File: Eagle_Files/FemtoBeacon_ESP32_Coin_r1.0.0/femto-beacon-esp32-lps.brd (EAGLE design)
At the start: 54.6 x 33 mm, 56 parts, among them IC1 ESP32-QFN_5X5

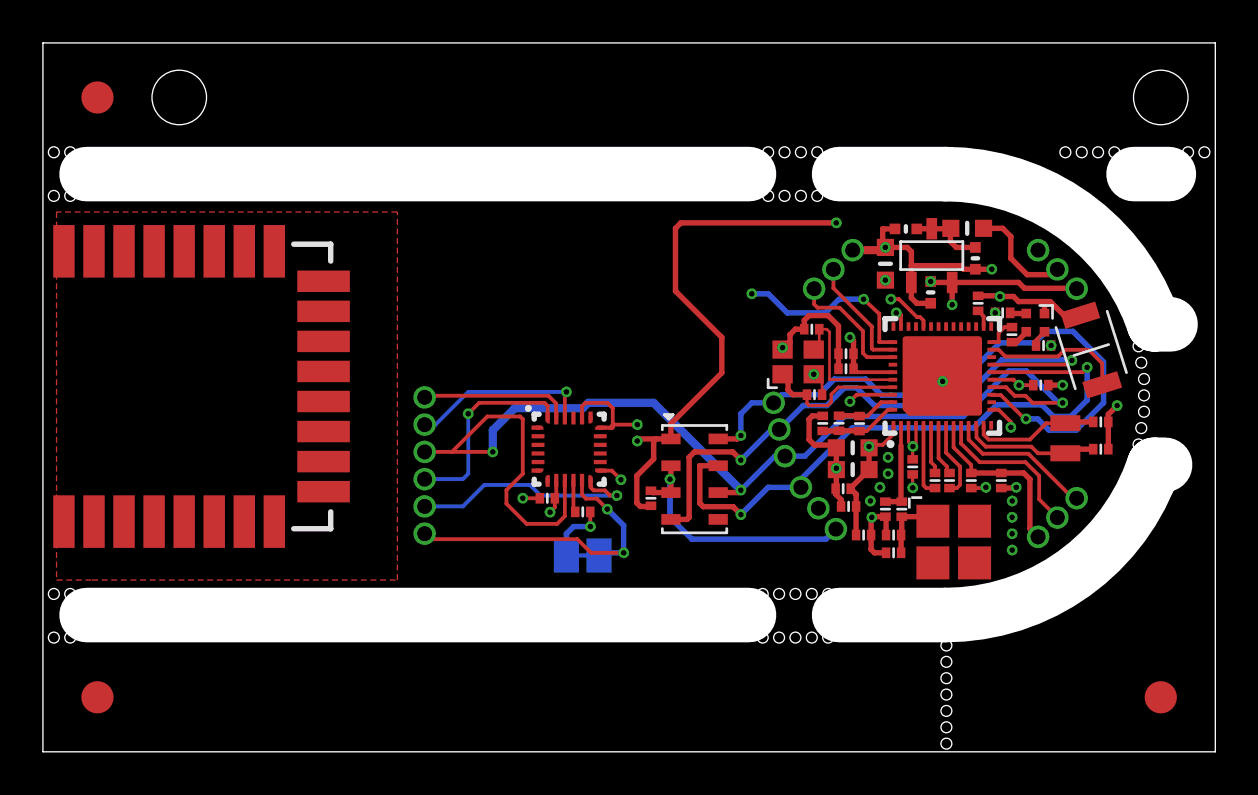
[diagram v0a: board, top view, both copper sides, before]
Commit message: Updating ESP32-WROOM-32 board. RGB Blue pin reassigned, and RGB pin 1 set to VCC instead of GND. LiPo connector pins were switched, corrected now.
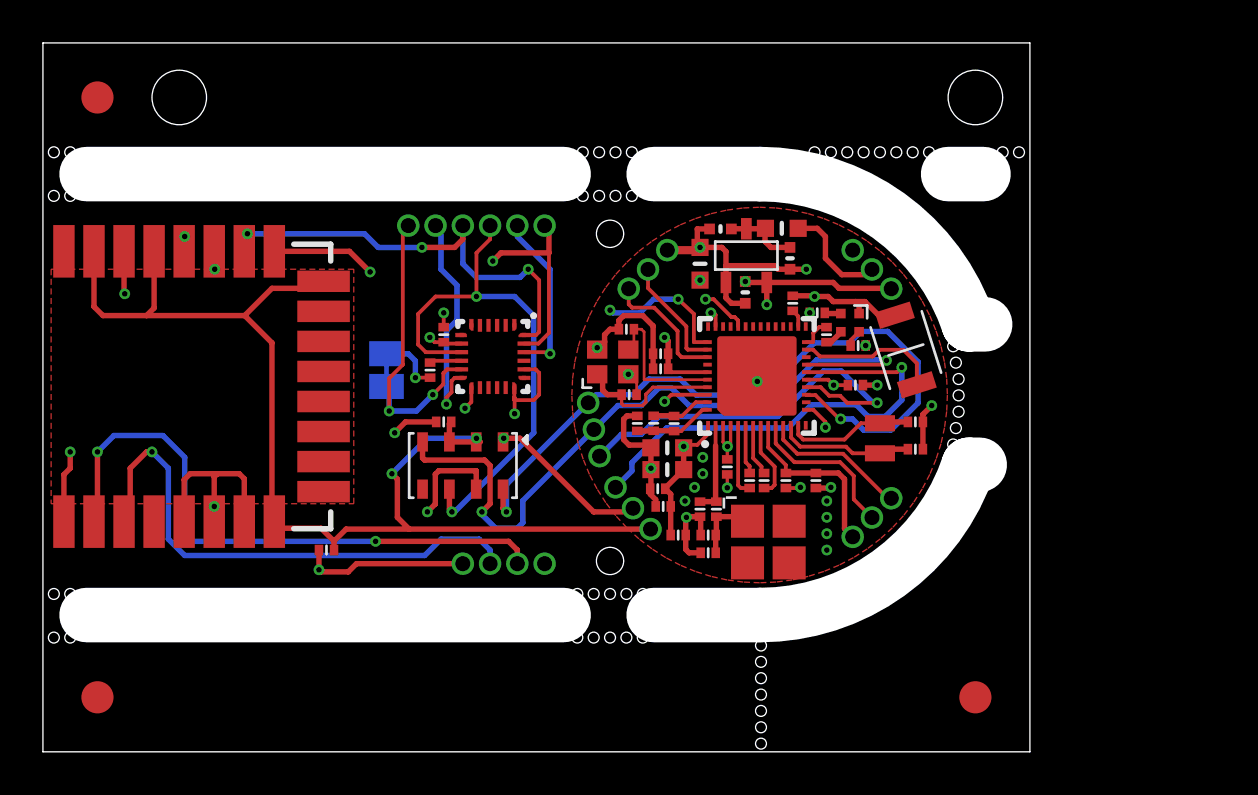
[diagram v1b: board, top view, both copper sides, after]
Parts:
- removed U$41: ICM-20948, icm-20948:QFN24_3X3
- removed U$9: MS5611-01BA03, freeimu:MS5611-01BA03
- added ALT1: MS5611-01BA03, freeimu:MS5611-01BA03
- added IMU1: ICM-20948, icm-20948:QFN24_3X3
- added R7: 4.7K, parts_0201:PART
- added U$39: 1X4_ROUND, pins_1.27mm_pitch:1X4_ROUND
- R6: value DNP -> 0
- moved SJ_FSYNC 12.6 mm to (16.0, 17.8), turned to 90 degrees
- moved C25 10.3 mm to (18.7, 15.4), turned to 0 degrees
- moved PIN_IMU_SPI 9.76 mm to (23.4, 24.5), turned to 270 degrees
- moved C29 9.71 mm to (18.0, 17.8), turned to 90 degrees
- moved C28 9.02 mm to (18.7, 19.4), turned to 270 degrees
- moved ANT1 8.64 mm to (33.8, 9.78)
- moved C1 8.64 mm to (28.6, 12.3)
- moved C10 8.64 mm to (29.1, 14.2)
- moved C11 8.64 mm to (29.1, 13.1)
- moved C12 8.64 mm to (28.9, 11.4)
- moved C15 8.64 mm to (28.8, 17.8)
- moved C16 8.64 mm to (28.8, 18.5)
- moved C18 8.64 mm to (34.9, 20.9)
- moved C19 8.64 mm to (37.8, 17.1)
- moved C20 8.64 mm to (27.7, 15.3)
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- renumbered U$50 to LPS1
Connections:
- new net EXTON_DECA: LPS1.1, U$39.P$1
- new net IRQ_DECA: LPS1.22, R7.1, U$39.P$4
- new net RST_DECA: LPS1.3, U$39.P$3
- new net WAKE_DECA: LPS1.2, U$39.P$2
- net 3.3V: now also ALT1.1, IMU1.13, IMU1.8, LPS1.5, LPS1.6, LPS1.7; no longer U$41.13, U$41.8, U$9.1
- net FSYNC_IMU: now also IMU1.11; no longer U$41.11
- net GND: now also ALT1.2, ALT1.3, IMU1.18, IMU1.20, LPS1.16, LPS1.21, LPS1.23, LPS1.24, LPS1.8, R7.2; no longer U$41.18, U$41.20, U$9.2, U$9.3
- net INT_WAKE_IMU: now also IMU1.12; no longer U$41.12
- net MTCK/HSPID(MOSI): now also ALT1.7, IMU1.24, LPS1.18; no longer U$41.24, U$9.7
- net MTDI/HSPIQ(MISO): now also ALT1.6, IMU1.9, LPS1.19; no longer U$41.9, U$9.6
- net MTDO/HSPICS0(CS): now also ALT1.4, IMU1.22, LPS1.17; no longer U$41.22, U$9.4
- net MTMS/HSPI_CLK: now also ALT1.8, IMU1.23, LPS1.20; no longer U$41.23, U$9.8
- net N$16: now also IMU1.10; no longer U$41.10
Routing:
- net GND: track 117.8 -> 158.2 mm, vias 16 -> 17
- net IRQ_DECA: track 0.00 -> 30.6 mm, vias 0 -> 2
- net EXTON_DECA: track 0.00 -> 29.9 mm, vias 0 -> 1
- net WAKE_DECA: track 0.00 -> 28.1 mm, vias 0 -> 2
- net RST_DECA: track 0.00 -> 24.8 mm, vias 0 -> 1
- net MTMS/HSPI_CLK: track 52.9 -> 74.7 mm, vias 2 -> 4
- net MTCK/HSPID(MOSI): track 57.5 -> 74.2 mm, vias 3 -> 5
- net MTDO/HSPICS0(CS): track 53.2 -> 68.5 mm, vias 3 -> 4
- net MTDI/HSPIQ(MISO): track 53.8 -> 66.4 mm, vias 3 -> 4
- net EN_1.8V: track 8.79 -> 6.44 mm
- net 3.3V: track 100.0 -> 101.9 mm, vias 13 -> 14
- net INT_WAKE_IMU: track 11.3 -> 10.6 mm
- net FSYNC_IMU: track 15.3 -> 14.7 mm
- removed copper zone on layer 2, net GND
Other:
- board size 54.6 x 33 mm -> 46 x 33 mm
- board text added: "LPS/WiFi/BT"
- board text added: "https://femto.io"

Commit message: Fixing solder stop mask on femto-beacon-esp32coin and femto-beacon-esp32-lps. Adding Blender3D model of stencil jig for the coin
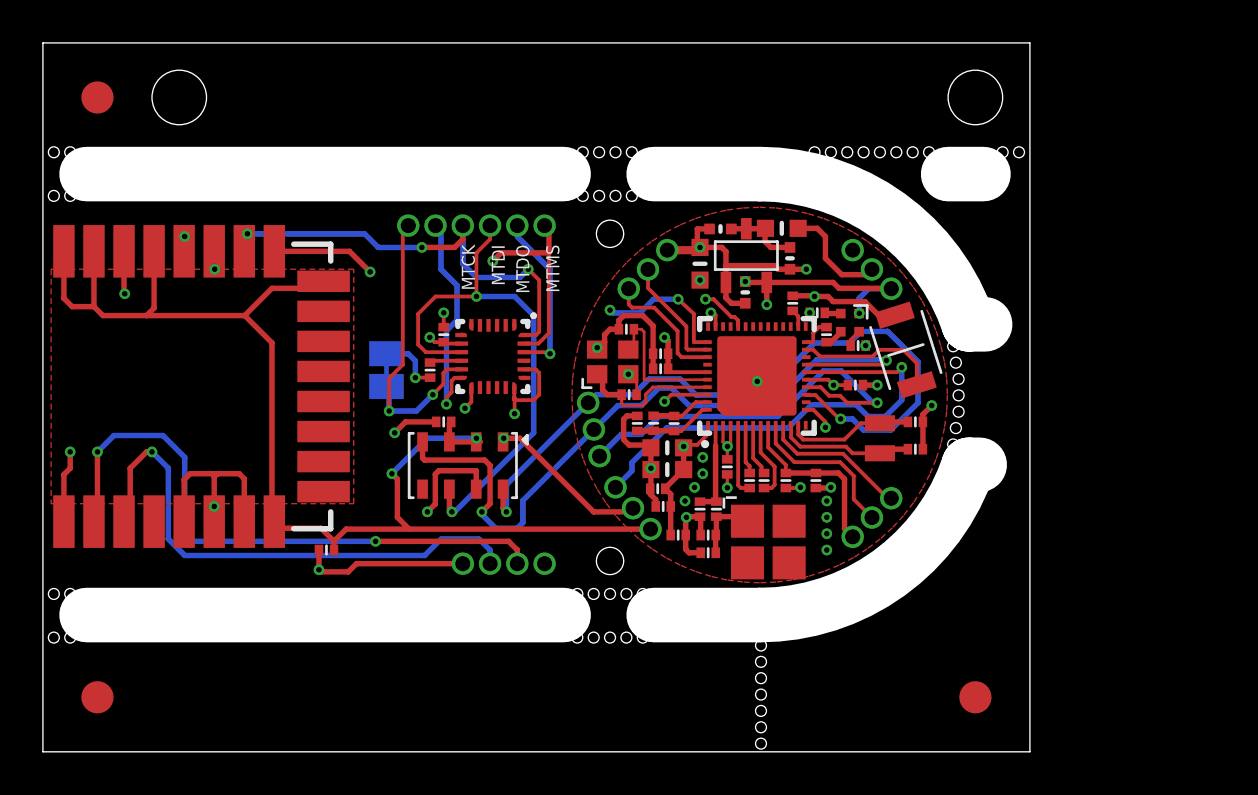
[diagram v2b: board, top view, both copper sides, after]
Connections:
- net B renamed IO5/B
- net G renamed IO4/G
- net R renamed IO26/R
- net 3.3V: now also RGB1.1
- net GND: no longer RGB1.1
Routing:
- net GND: track 158.2 -> 161.3 mm
- net 3.3V: track 101.9 -> 104.3 mm, vias 14 -> 15
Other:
- board text added: "1.0.1"
- board text added: "EN"
- board text added: "IO34"
- board text added: "IO35"
- board text added: "LPS/EXTON"
- board text added: "LPS/IRQ"
- board text added: "LPS/RST"
- board text added: "LPS/WAKE"
- board text added: "MTCK"
- board text added: "MTDI"
- board text added: "MTDO"
- board text added: "MTMS"
- board text added: "SPI (3.3V)"
- board text removed: "1.0.0"
- board text removed: "SPI (1.8V)"
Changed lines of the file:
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@@
 <setting verticaltext="up"/>
 </settings>
-<grid distance="30" unitdist="mil" unit="mil" style="dots" multiple="1" display="yes" altdistance="5" altunitdist="mil" altunit="mil"/>
+<grid distance="5" unitdist="mil" unit="mil" style="dots" multiple="1" display="yes" altdistance="5" altunitdist="mil" altunit="mil"/>
 <layers>
 <layer number="1" name="Top" color="4" fill="1" visible="yes" active="yes"/>
@@
 <text x="10.033" y="17.399" size="0.8128" layer="22" font="vector" ratio="20" rot="MR270" align="center">FemtoBeacon</text>
 <text x="8.89" y="17.399" size="0.8128" layer="22" font="vector" ratio="20" rot="MR270" align="center">ESP32 LPS</text>
-<text x="33.782" y="9.652" size="0.8128" layer="22" font="vector" ratio="20" rot="MR0" align="center">1.0.0</text>
+<text x="33.782" y="9.652" size="0.8128" layer="22" font="vector" ratio="20" rot="MR0" align="center">1.0.1</text>
 <text x="33.528" y="19.05" size="0.8128" layer="22" font="vector" ratio="20" rot="MR0" align="center">IO26=R</text>
 <text x="33.528" y="18.034" size="0.8128" layer="22" font="vector" ratio="20" rot="MR0" align="center">IO4=G</text>
@@
 <text x="17.018" y="23.622" size="0.6096" layer="22" font="vector" ratio="20" rot="MR270" align="center-left">FSYNC</text>
 <text x="15.494" y="22.987" size="0.6096" layer="22" font="vector" ratio="20" rot="MR90" align="center">SPI
-(1.8V)</text>
+(3.3V)</text>
 <text x="16.002" y="20.574" size="0.6096" layer="22" font="vector" ratio="20" rot="MR0" align="center">GND</text>
 <text x="16.256" y="15.24" size="0.6096" layer="22" font="vector" ratio="20" rot="MR0" align="center">FSYNC</text>
@@
 <hole x="36.703" y="27.9271" drill="0.508"/>
 <hole x="35.941" y="27.9271" drill="0.508"/>
+<text x="38.608" y="12.573" size="0.6096" layer="22" font="vector" ratio="20" rot="MR45" align="center-left">IO35</text>
+<text x="37.846" y="11.811" size="0.6096" layer="22" font="vector" ratio="20" rot="MR45" align="center-left">IO34</text>
+<text x="37.084" y="11.049" size="0.6096" layer="22" font="vector" ratio="20" rot="MR45" align="center-left">EN</text>
+<text x="23.368" y="9.779" size="0.6096" layer="22" font="vector" ratio="20" rot="MR90" align="center-left">LPS/EXTON</text>
+<text x="22.098" y="9.652" size="0.6096" layer="22" font="vector" ratio="20" rot="MR90" align="center-left">LPS/WAKE</text>
+<text x="20.828" y="9.652" size="0.6096" layer="22" font="vector" ratio="20" rot="MR90" align="center-left">LPS/RST</text>
+<text x="19.558" y="9.652" size="0.6096" layer="22" font="vector" ratio="20" rot="MR90" align="center-left">LPS/IRQ</text>
+<text x="23.749" y="23.622" size="0.6096" layer="21" font="vector" ratio="20" rot="R270" align="center-left">MTMS</text>
+<text x="22.352" y="23.622" size="0.6096" layer="21" font="vector" ratio="20" rot="R270" align="center-left">MTDO</text>
+<text x="21.209" y="23.622" size="0.6096" layer="21" font="vector" ratio="20" rot="R270" align="center-left">MTDI</text>
+<text x="19.812" y="23.622" size="0.6096" layer="21" font="vector" ratio="20" rot="R270" align="center-left">MTCK</text>
 </plain>
 <attributes>
@@
 <wire x1="39.6843" y1="20.33681875" x2="38.9223" y2="20.33681875" width="0.254" layer="1"/>
 <wire x1="38.9223" y1="20.33681875" x2="38.2873" y2="20.97181875" width="0.254" layer="1"/>
-<wire x1="38.2873" y1="20.97181875" x2="37.846" y2="20.97181875" width="0.254" layer="1"/>
-<wire x1="37.846" y1="20.97181875" x2="36.81318125" y2="20.97181875" width="0.254" layer="1"/>
+<wire x1="38.2873" y1="20.97181875" x2="36.81318125" y2="20.97181875" width="0.254" layer="1"/>
 <wire x1="36.81318125" y1="20.97181875" x2="36.576" y2="21.209" width="0.254" layer="1"/>
 <wire x1="36.576" y1="21.209" x2="35.941" y2="21.209" width="0.254" layer="1"/>
@@
 <wire x1="28.321" y1="13.1445" x2="28.321" y2="13.208" width="0.254" layer="1"/>
 <wire x1="33.274" y1="17.255" x2="33.274" y2="12.2989" width="0.381" layer="2"/>
-<contactref element="RGB1" pad="1"/>
-<wire x1="38.017" y1="20.4148" x2="38.017" y2="20.80081875" width="0.254" layer="1"/>
-<wire x1="38.017" y1="20.80081875" x2="37.846" y2="20.97181875" width="0.254" layer="1"/>
 <contactref element="PIN_GPIO_A" pad="P$3"/>
 <wire x1="28.302678125" y1="10.373246875" x2="28.534246875" y2="10.373246875" width="0.381" layer="2"/>
@@
 <wire x1="17.3482" y1="15.9258" x2="17.3482" y2="17.4244" width="0.381" layer="2"/>
 <wire x1="18.669" y1="14.605" x2="17.3482" y2="15.9258" width="0.381" layer="2"/>
+<wire x1="0.978" y1="23.313" x2="0.978" y2="21.12" width="0.254" layer="1"/>
+<wire x1="1.362" y1="20.736" x2="2.378" y2="20.736" width="0.254" layer="1"/>
+<wire x1="0.978" y1="21.12" x2="1.362" y2="20.736" width="0.254" layer="1"/>
 </signal>
 <signal name="XOUT">
@@
 <wire x1="22.225" y1="14.605" x2="21.603" y2="14.605" width="0.254" layer="1"/>
 <wire x1="21.603" y1="14.605" x2="21.433" y2="14.435" width="0.254" layer="1"/>
+<contactref element="RGB1" pad="1"/>
+<wire x1="38.017" y1="20.4148" x2="38.027" y2="20.4248" width="0.254" layer="1"/>
+<via x="38.027" y="20.4248" extent="1-16" drill="0.254" diameter="0.508"/>
+<wire x1="38.027" y1="20.4248" x2="38.027" y2="21.136" width="0.254" layer="16"/>
+<wire x1="38.462946875" y1="21.571946875" x2="39.51505" y2="21.571946875" width="0.254" layer="16"/>
+<wire x1="38.027" y1="21.136" x2="38.462946875" y2="21.571946875" width="0.254" layer="16"/>
 </signal>
 <signal name="VIN_PIN">
@@
 <contactref element="IC1" pad="16"/>
 </signal>
-<signal name="R">
+<signal name="IO26/R">
 <contactref element="R5" pad="2"/>
 <via x="38.323" y="18.923" extent="1-16" drill="0.254" diameter="0.508"/>
@@
 <wire x1="38.227" y1="14.605" x2="38.227" y2="15.621" width="0.254" layer="15"/>
 </signal>
-<signal name="G">
+<signal name="IO4/G">
 <contactref element="R4" pad="2"/>
 <contactref element="IC1" pad="24"/>
@@
 <wire x1="36.15455" y1="19.781" x2="36.4998" y2="19.781" width="0.1778" layer="1"/>
 </signal>
-<signal name="B">
+<signal name="IO5/B">
 <contactref element="R3" pad="2"/>
 <via x="35.718" y="20.447" extent="1-16" drill="0.254" diameter="0.508"/>
